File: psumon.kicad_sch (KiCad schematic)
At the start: 4 parts, among them U8 INA260

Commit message: work on control logic
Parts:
- renumbered C12 to C14, C13 to C15, U8 to U9
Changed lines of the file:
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@@
   (symbol (lib_id "power:GND") (at 125.73 90.17 0) (unit 1)
     (in_bom yes) (on_board yes)
-    (property "Reference" "#PWR?" (id 0) (at 125.73 96.52 0)
+    (property "Reference" "#PWR024" (id 0) (at 125.73 96.52 0)
       (effects (font (size 1.27 1.27)) hide)
     )
@@
   (symbol (lib_id "Device:C_Small") (at 58.42 58.42 0) (unit 1)
     (in_bom yes) (on_board yes) (fields_autoplaced)
-    (property "Reference" "C12" (id 0) (at 60.96 57.1562 0)
+    (property "Reference" "C14" (id 0) (at 60.96 57.1562 0)
       (effects (font (size 1.27 1.27)) (justify left))
     )
@@
   (symbol (lib_id "power:GND") (at 69.85 68.58 0) (unit 1)
     (in_bom yes) (on_board yes) (fields_autoplaced)
-    (property "Reference" "#PWR?" (id 0) (at 69.85 74.93 0)
+    (property "Reference" "#PWR023" (id 0) (at 69.85 74.93 0)
       (effects (font (size 1.27 1.27)) hide)
     )
@@
   (symbol (lib_id "Sensor_I2C_TI:INA260") (at 125.73 67.31 0) (mirror y) (unit 1)
     (in_bom yes) (on_board yes)
-    (property "Reference" "U8" (id 0) (at 120.015 58.42 0))
+    (property "Reference" "U9" (id 0) (at 120.015 58.42 0))
     (property "Value" "INA260" (id 1) (at 131.445 76.2 0))
     (property "Footprint" "Sensor_I2C_TI:TSSOP-16_4.4x5mm_P0.65mm_pin1" (id 2) (at 124.46 99.06 0)
@@
   (symbol (lib_id "Device:C_Small") (at 69.85 58.42 0) (unit 1)
     (in_bom yes) (on_board yes) (fields_autoplaced)
-    (property "Reference" "C13" (id 0) (at 72.39 57.1562 0)
+    (property "Reference" "C15" (id 0) (at 72.39 57.1562 0)
       (effects (font (size 1.27 1.27)) (justify left))
     )

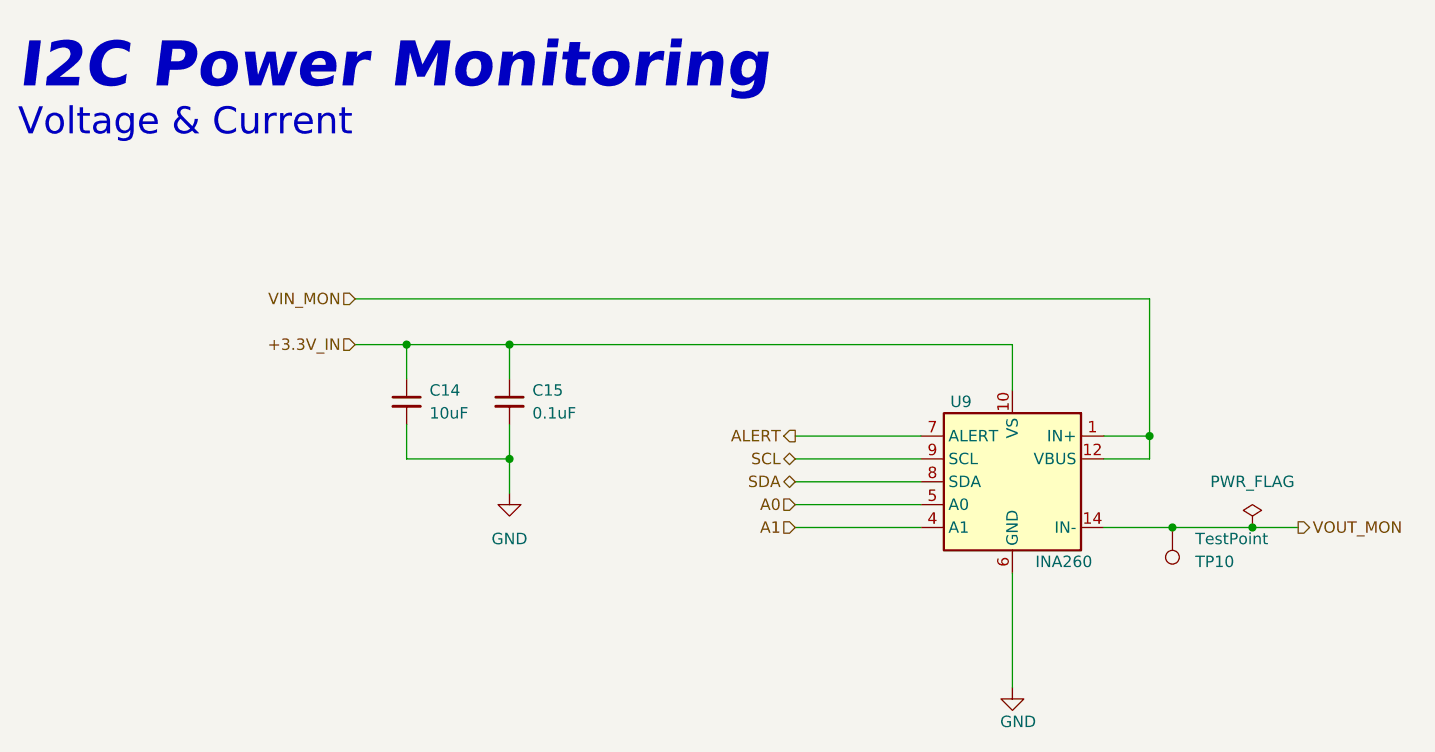
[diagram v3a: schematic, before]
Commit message: connecterized faceplate, refreshed schematic
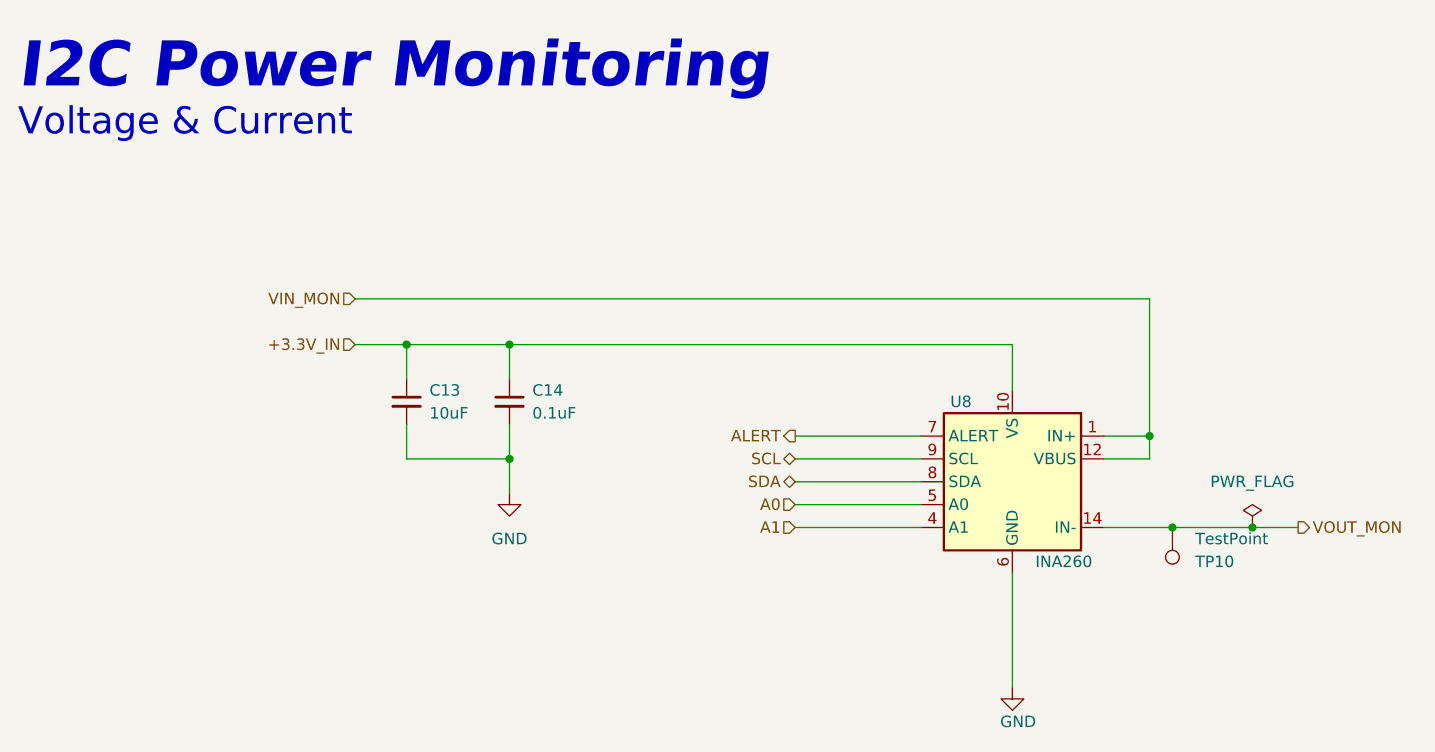
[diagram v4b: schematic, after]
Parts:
- renumbered C14 to C13, C15 to C14, U9 to U8
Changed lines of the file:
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@@
   (symbol (lib_id "power:GND") (at 125.73 90.17 0)
     (in_bom yes) (on_board yes)
-    (property "Reference" "#PWR024" (id 0) (at 125.73 96.52 0)
+    (property "Reference" "#PWR023" (id 0) (at 125.73 96.52 0)
       (effects (font (size 1.27 1.27)) hide)
     )
@@
   (symbol (lib_id "Device:C_Small") (at 58.42 58.42 0)
     (in_bom yes) (on_board yes) (fields_autoplaced)
-    (property "Reference" "C14" (id 0) (at 60.96 57.1562 0)
+    (property "Reference" "C13" (id 0) (at 60.96 57.1562 0)
       (effects (font (size 1.27 1.27)) (justify left))
     )
@@
   (symbol (lib_id "power:GND") (at 69.85 68.58 0)
     (in_bom yes) (on_board yes) (fields_autoplaced)
-    (property "Reference" "#PWR023" (id 0) (at 69.85 74.93 0)
+    (property "Reference" "#PWR022" (id 0) (at 69.85 74.93 0)
       (effects (font (size 1.27 1.27)) hide)
     )
@@
   (symbol (lib_id "Sensor_I2C_TI:INA260") (at 125.73 67.31 0) (mirror y)
     (in_bom yes) (on_board yes)
-    (property "Reference" "U9" (id 0) (at 120.015 58.42 0))
+    (property "Reference" "U8" (id 0) (at 120.015 58.42 0))
     (property "Value" "INA260" (id 1) (at 131.445 76.2 0))
     (property "Footprint" "Sensor_I2C_TI:TSSOP-16_4.4x5mm_P0.65mm_pin1" (id 2) (at 124.46 99.06 0)
@@
   (symbol (lib_id "Device:C_Small") (at 69.85 58.42 0)
     (in_bom yes) (on_board yes) (fields_autoplaced)
-    (property "Reference" "C15" (id 0) (at 72.39 57.1562 0)
+    (property "Reference" "C14" (id 0) (at 72.39 57.1562 0)
       (effects (font (size 1.27 1.27)) (justify left))
     )

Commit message: trued up facecm4 connector pinout
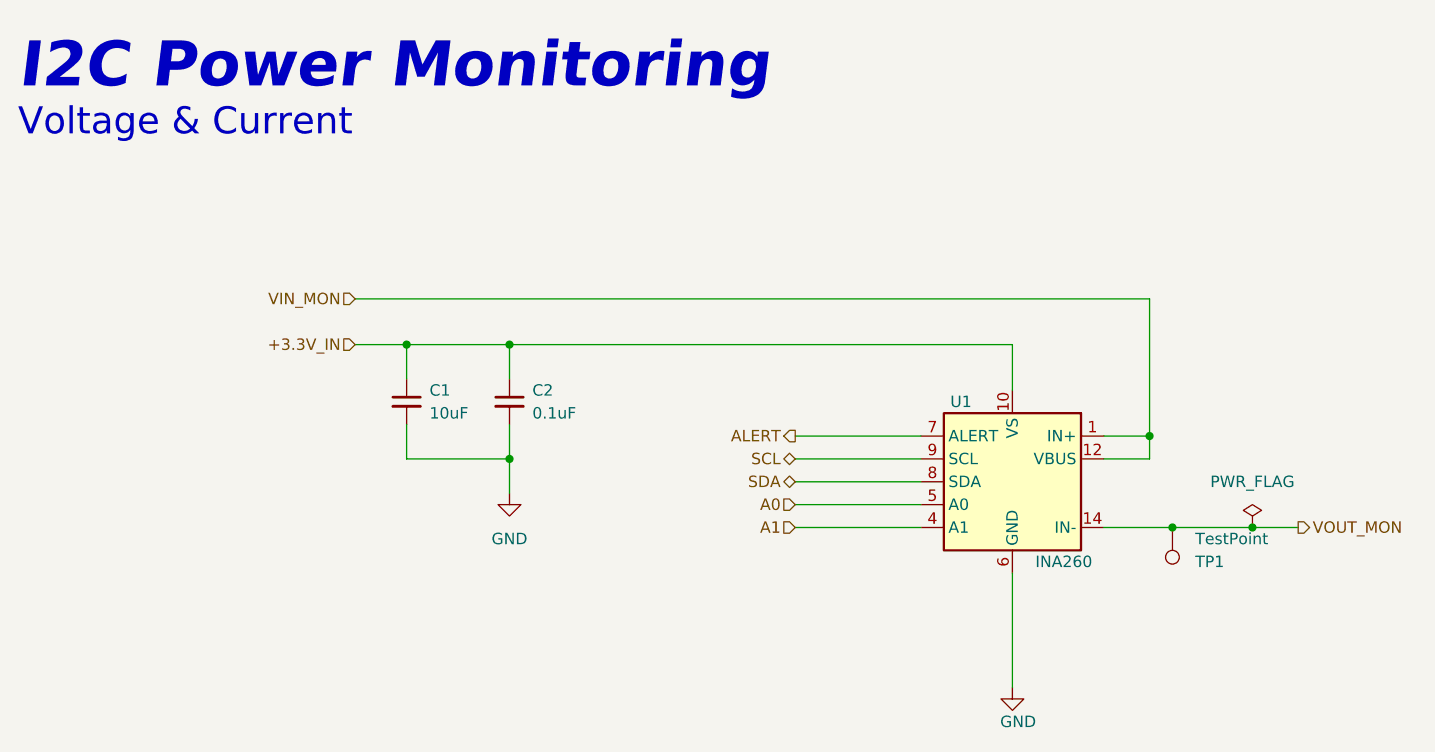
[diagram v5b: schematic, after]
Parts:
- renumbered C13 to C1, C14 to C2, TP10 to TP1, U8 to U1
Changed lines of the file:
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@@
   (symbol (lib_id "power:GND") (at 125.73 90.17 0)
     (in_bom yes) (on_board yes)
-    (property "Reference" "#PWR023" (id 0) (at 125.73 96.52 0)
+    (property "Reference" "#PWR03" (id 0) (at 125.73 96.52 0)
       (effects (font (size 1.27 1.27)) hide)
     )
@@
   (symbol (lib_id "Device:C_Small") (at 58.42 58.42 0)
     (in_bom yes) (on_board yes) (fields_autoplaced)
-    (property "Reference" "C13" (id 0) (at 60.96 57.1562 0)
+    (property "Reference" "C1" (id 0) (at 60.96 57.1562 0)
       (effects (font (size 1.27 1.27)) (justify left))
     )
@@
   (symbol (lib_id "power:GND") (at 69.85 68.58 0)
     (in_bom yes) (on_board yes) (fields_autoplaced)
-    (property "Reference" "#PWR022" (id 0) (at 69.85 74.93 0)
+    (property "Reference" "#PWR02" (id 0) (at 69.85 74.93 0)
       (effects (font (size 1.27 1.27)) hide)
     )
@@
   (symbol (lib_id "Sensor_I2C_TI:INA260") (at 125.73 67.31 0) (mirror y)
     (in_bom yes) (on_board yes)
-    (property "Reference" "U8" (id 0) (at 120.015 58.42 0))
+    (property "Reference" "U1" (id 0) (at 120.015 58.42 0))
     (property "Value" "INA260" (id 1) (at 131.445 76.2 0))
     (property "Footprint" "Sensor_I2C_TI:TSSOP-16_4.4x5mm_P0.65mm_pin1" (id 2) (at 124.46 99.06 0)
@@
   (symbol (lib_id "power:PWR_FLAG") (at 152.4 72.39 0)
     (in_bom yes) (on_board yes) (fields_autoplaced)
-    (property "Reference" "#FLG04" (id 0) (at 152.4 70.485 0)
+    (property "Reference" "#FLG03" (id 0) (at 152.4 70.485 0)
       (effects (font (size 1.27 1.27)) hide)
     )
@@
   (symbol (lib_id "Device:C_Small") (at 69.85 58.42 0)
     (in_bom yes) (on_board yes) (fields_autoplaced)
-    (property "Reference" "C14" (id 0) (at 72.39 57.1562 0)
+    (property "Reference" "C2" (id 0) (at 72.39 57.1562 0)
       (effects (font (size 1.27 1.27)) (justify left))
     )
@@
   (symbol (lib_id "Connector:TestPoint") (at 143.51 72.39 0) (mirror x)
     (in_bom yes) (on_board yes)
-    (property "Reference" "TP10" (id 0) (at 146.05 76.2 0)
+    (property "Reference" "TP1" (id 0) (at 146.05 76.2 0)
       (effects (font (size 1.27 1.27)) (justify left))
     )

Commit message: leds
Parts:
- renumbered C1 to C13, C2 to C14, TP1 to TP10, U1 to U8
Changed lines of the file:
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@@
   (symbol (lib_id "power:GND") (at 125.73 90.17 0)
     (in_bom yes) (on_board yes)
-    (property "Reference" "#PWR03" (id 0) (at 125.73 96.52 0)
+    (property "Reference" "#PWR023" (id 0) (at 125.73 96.52 0)
       (effects (font (size 1.27 1.27)) hide)
     )
@@
   (symbol (lib_id "Device:C_Small") (at 58.42 58.42 0)
     (in_bom yes) (on_board yes) (fields_autoplaced)
-    (property "Reference" "C1" (id 0) (at 60.96 57.1562 0)
+    (property "Reference" "C13" (id 0) (at 60.96 57.1562 0)
       (effects (font (size 1.27 1.27)) (justify left))
     )
@@
   (symbol (lib_id "power:GND") (at 69.85 68.58 0)
     (in_bom yes) (on_board yes) (fields_autoplaced)
-    (property "Reference" "#PWR02" (id 0) (at 69.85 74.93 0)
+    (property "Reference" "#PWR022" (id 0) (at 69.85 74.93 0)
       (effects (font (size 1.27 1.27)) hide)
     )
@@
   (symbol (lib_id "Sensor_I2C_TI:INA260") (at 125.73 67.31 0) (mirror y)
     (in_bom yes) (on_board yes)
-    (property "Reference" "U1" (id 0) (at 120.015 58.42 0))
+    (property "Reference" "U8" (id 0) (at 120.015 58.42 0))
     (property "Value" "INA260" (id 1) (at 131.445 76.2 0))
     (property "Footprint" "Sensor_I2C_TI:TSSOP-16_4.4x5mm_P0.65mm_pin1" (id 2) (at 124.46 99.06 0)
@@
   (symbol (lib_id "power:PWR_FLAG") (at 152.4 72.39 0)
     (in_bom yes) (on_board yes) (fields_autoplaced)
-    (property "Reference" "#FLG03" (id 0) (at 152.4 70.485 0)
+    (property "Reference" "#FLG04" (id 0) (at 152.4 70.485 0)
       (effects (font (size 1.27 1.27)) hide)
     )
@@
   (symbol (lib_id "Device:C_Small") (at 69.85 58.42 0)
     (in_bom yes) (on_board yes) (fields_autoplaced)
-    (property "Reference" "C2" (id 0) (at 72.39 57.1562 0)
+    (property "Reference" "C14" (id 0) (at 72.39 57.1562 0)
       (effects (font (size 1.27 1.27)) (justify left))
     )
@@
   (symbol (lib_id "Connector:TestPoint") (at 143.51 72.39 0) (mirror x)
     (in_bom yes) (on_board yes)
-    (property "Reference" "TP1" (id 0) (at 146.05 76.2 0)
+    (property "Reference" "TP10" (id 0) (at 146.05 76.2 0)
       (effects (font (size 1.27 1.27)) (justify left))
     )
